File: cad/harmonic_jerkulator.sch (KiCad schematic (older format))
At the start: 41 parts, among them J101 JACK_IN, J102 JACK_OUT, J103 CONN_PSU, J105 PNP, J106 NPN, J107 SW_BYPASS, J108 DIODE1, J109 SW_DIODE, J110 DIODE2, J111 CONN_CONN_BOARD, J112 SW_DIODE, J113 CONN_CIRCUIT_BOARD, K101 TQ2SA-5V, Q101 BC850, Q102 BC856, Q103 DTC123Y, Q104 DTC123Y, U101 4013

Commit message: Corrected schematic : serial resistors on relay coil. Started layout.
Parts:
- added R112, R113: 150, Resistors_SMD:R_0805, symbol R
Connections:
- net labels removed: +BATT
- wire segments 137 -> 138
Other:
- moved on the sheet: D103, J107, K101, Q103, R106, R107, U101A

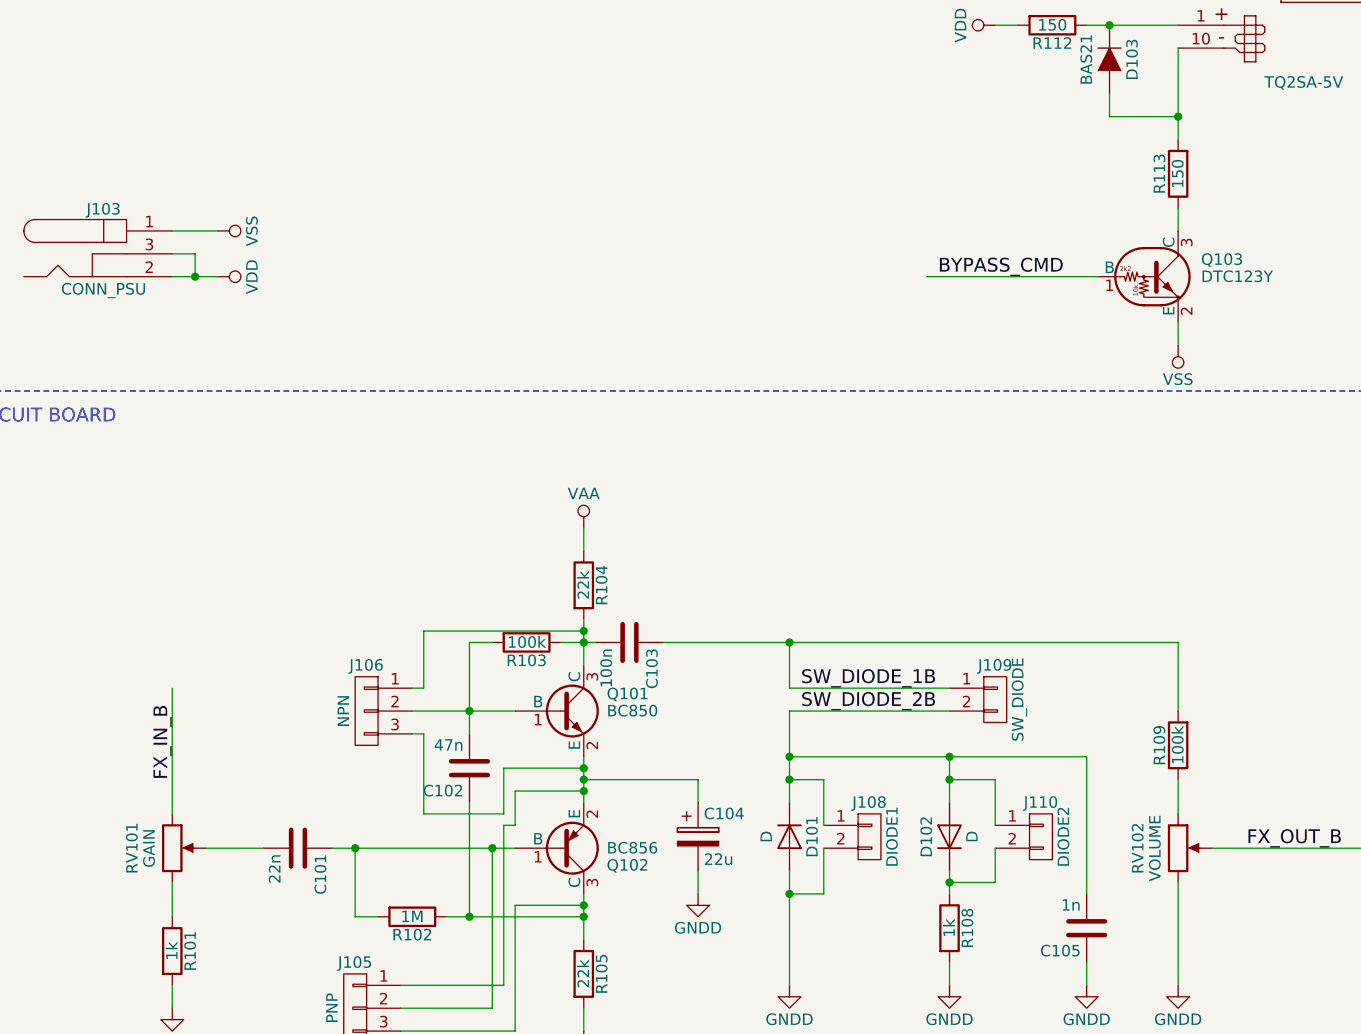
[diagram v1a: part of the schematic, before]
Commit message: Corrected pots polarity.
Connected GND and VSS.
Done single-side layout on Connectors board.
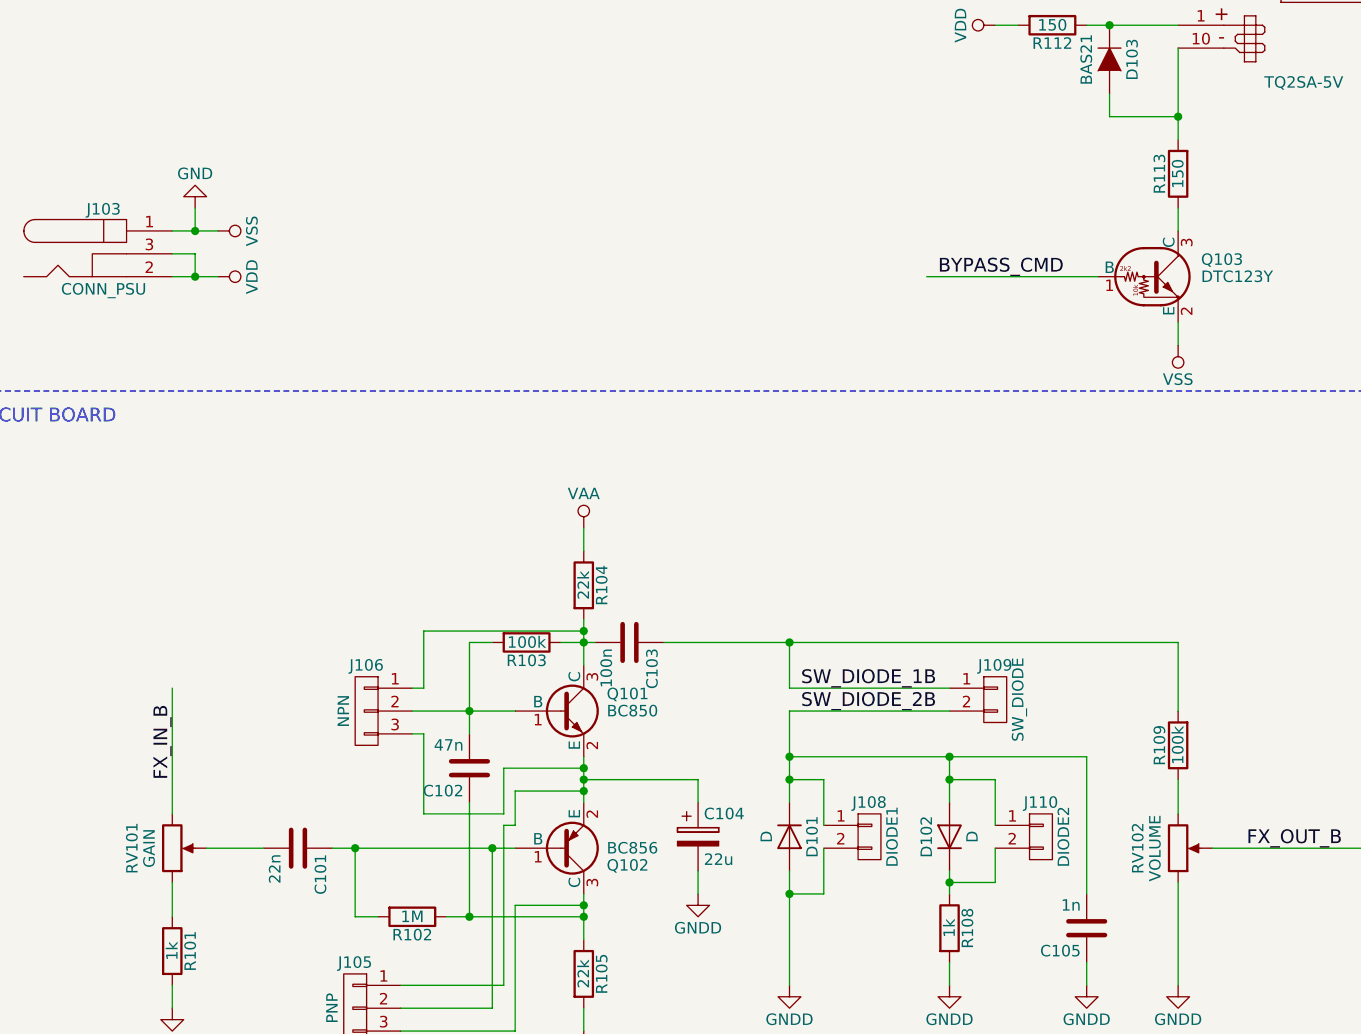
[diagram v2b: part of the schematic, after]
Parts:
- J103: footprint Connect:JACK_ALIM -> Connect:BARREL_JACK
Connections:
- wire segments 138 -> 139
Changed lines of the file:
@@
 LIBS:contrib
 LIBS:valves
+LIBS:flax_lib
 LIBS:harmonic_jerkulator-cache
 EELAYER 25 0
@@
 F 0 "J103" H 1200 3995 50  0000 C CNN
 F 1 "CONN_PSU" H 1200 3645 50  0000 C CNN
-F 2 "Connect:JACK_ALIM" H 1200 3800 50  0001 C CNN
+F 2 "Connect:BARREL_JACK" H 1200 3800 50  0001 C CNN
 F 3 "" H 1200 3800 50  0001 C CNN
 	1    1200 3800
@@
 F 3 "" H 1500 6400 50  0001 C CNN
 	1    1500 6400
-	1    0    0    -1
+	1    0    0    1
 $EndComp
 $Comp
@@
 F 3 "" H 5900 6400 50  0001 C CNN
 	1    5900 6400
-	1    0    0    -1
+	1    0    0    1
 $EndComp
 $Comp
@@
 	10500 5900 10400 5900
 Connection ~ 10400 5900
+$Comp
+L GND #PWR030
+U 1 1 59A57141
+P 1600 3600
+F 0 "#PWR030" H 1600 3350 50  0001 C CNN
+F 1 "GND" H 1600 3450 50  0000 C CNN
+F 2 "" H 1600 3600 50  0001 C CNN
+F 3 "" H 1600 3600 50  0001 C CNN
+	1    1600 3600
+	-1   0    0    1
+$EndComp
+Wire Wire Line
+	1600 3600 1600 3700
+Connection ~ 1600 3700
 $EndSCHEMATC

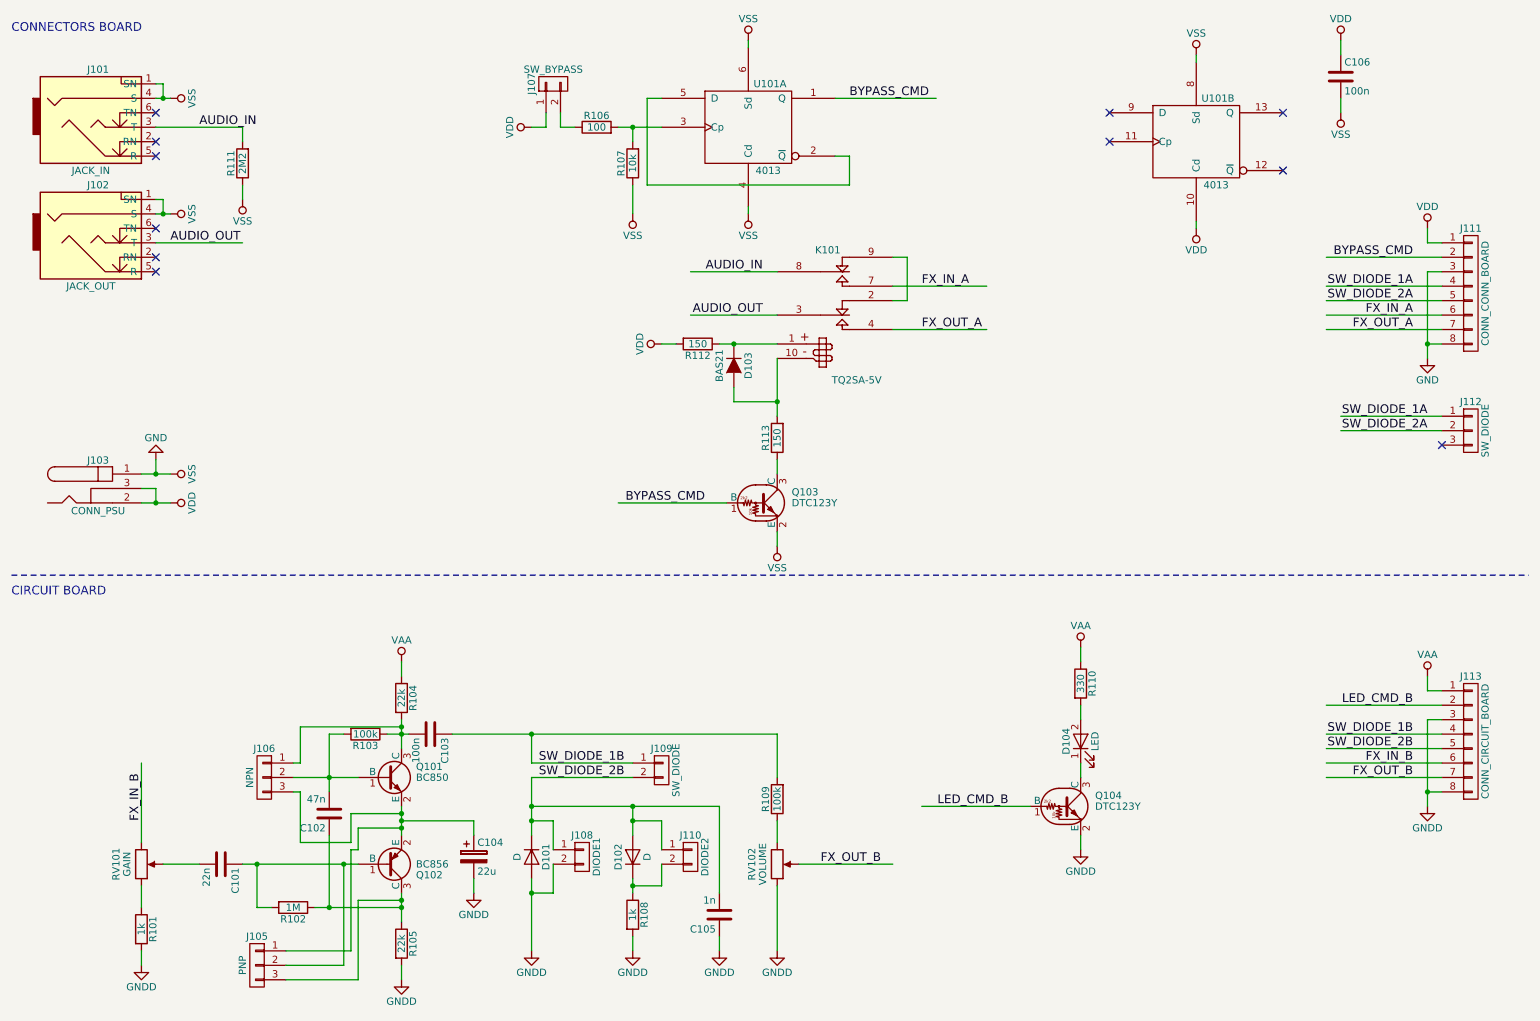
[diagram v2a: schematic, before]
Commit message: Corrections on schematic. Not finished.
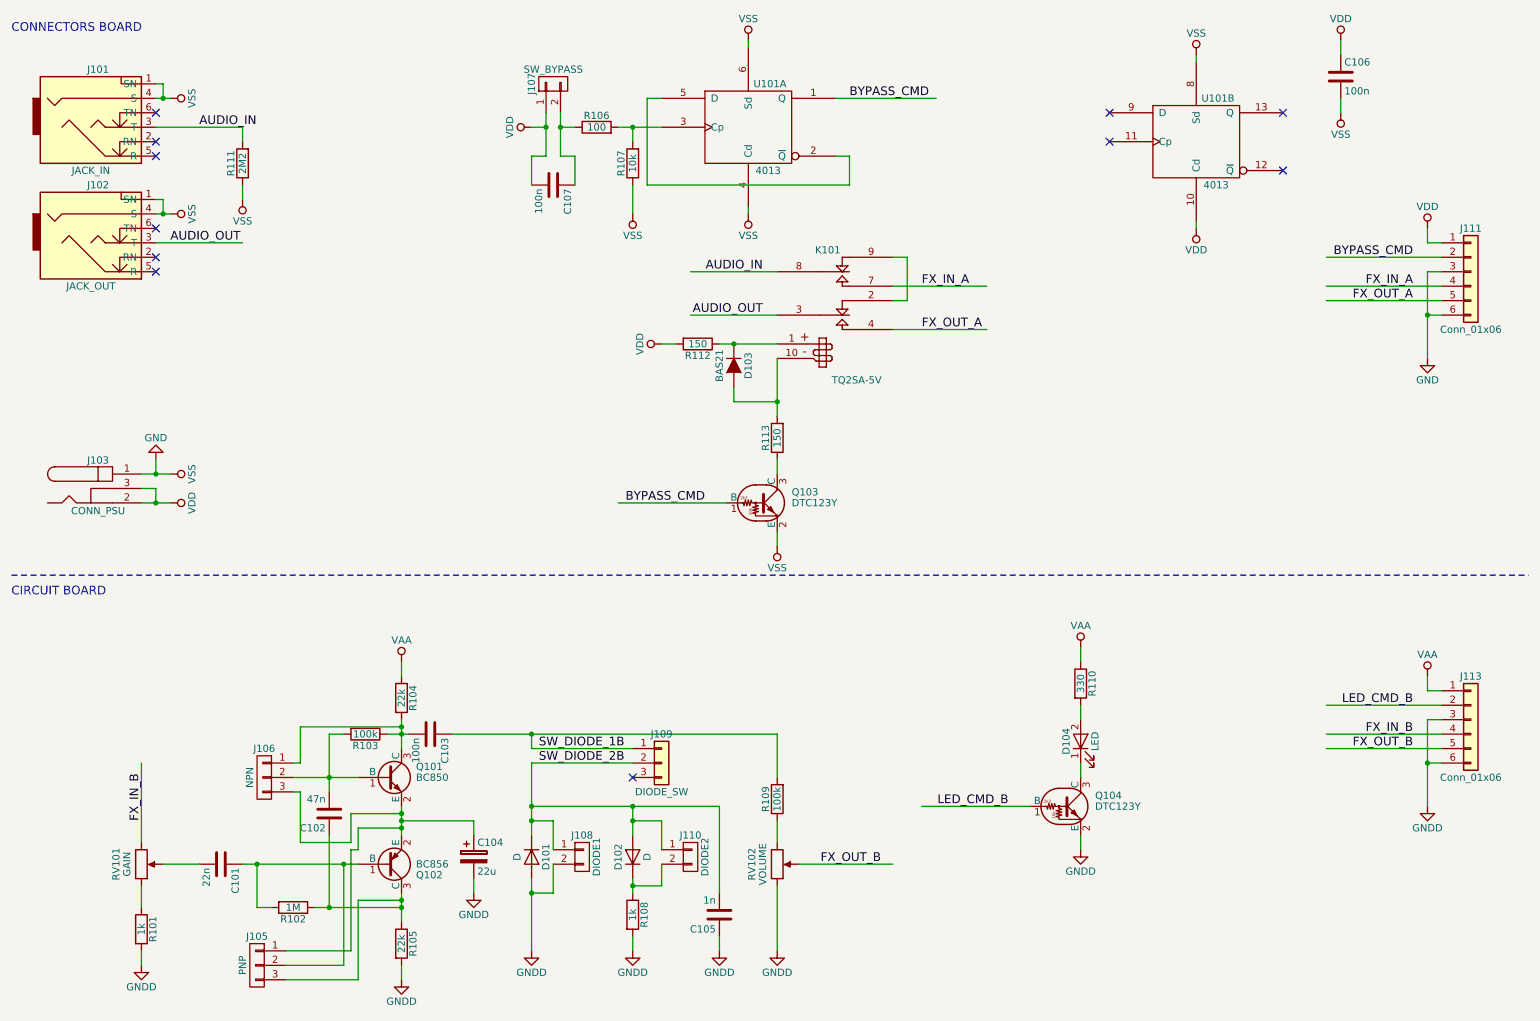
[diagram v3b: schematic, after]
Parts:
- removed J109: SW_DIODE, Pin_Headers:Pin_Header_Straight_1x02_Pitch2.54mm, symbol CONN_01X02
- removed J111: CONN_CONN_BOARD, Pin_Headers:Pin_Header_Straight_1x08_Pitch2.54mm, symbol CONN_01X08
- removed J112: SW_DIODE, Pin_Headers:Pin_Header_Straight_1x03_Pitch2.54mm, symbol CONN_01X03
- removed J113: CONN_CIRCUIT_BOARD, Pin_Headers:Pin_Header_Straight_1x08_Pitch2.54mm, symbol CONN_01X08
- added C107: 100n, Capacitors_SMD:C_0603, symbol C
- added J109: DIODE_SW, Pin_Headers:Pin_Header_Straight_1x03_Pitch2.54mm, symbol Conn_01x03
- added J111, J113: Conn_01x06, Pin_Headers:Pin_Header_Straight_1x06_Pitch2.54mm, symbol Conn_01x06
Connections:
- net labels removed: SW_DIODE_1A, SW_DIODE_2A
- wire segments 139 -> 137
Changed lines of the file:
@@
-$EndComp
-$Comp
-L CONN_01X08 J111
-U 1 1 599CA674
-P 10700 2450
-F 0 "J111" H 10700 2900 50  0000 C CNN
-F 1 "CONN_CONN_BOARD" V 10800 2450 50  0000 C CNN
-F 2 "Pin_Headers:Pin_Header_Straight_1x08_Pitch2.54mm" H 10700 2450 50  0001 C CNN
-F 3 "" H 10700 2450 50  0001 C CNN
-	1    10700 2450
-	1    0    0    -1
-$EndComp
-$Comp
-L CONN_01X08 J113
-U 1 1 599CA9F3
-P 10700 5550
-F 0 "J113" H 10700 6000 50  0000 C CNN
-F 1 "CONN_CIRCUIT_BOARD" V 10800 5550 50  0000 C CNN
-F 2 "Pin_Headers:Pin_Header_Straight_1x08_Pitch2.54mm" H 10700 5550 50  0001 C CNN
-F 3 "" H 10700 5550 50  0001 C CNN
-	1    10700 5550
-	1    0    0    -1
 $EndComp
 $Comp
@@
 Text Label 6200 6400 0    60   ~ 0
 FX_OUT_B
-Text Label 10300 5700 2    60   ~ 0
+Text Label 10300 5500 2    60   ~ 0
 FX_IN_B
-Text Label 10300 5800 2    60   ~ 0
+Text Label 10300 5600 2    60   ~ 0
 FX_OUT_B
 Text Label 10300 5300 2    60   ~ 0
@@
 	1    0    0    -1
 $EndComp
-Text Label 10300 2600 2    60   ~ 0
+Text Label 10300 2400 2    60   ~ 0
 FX_IN_A
-Text Label 10300 2700 2    60   ~ 0
+Text Label 10300 2500 2    60   ~ 0
 FX_OUT_A
 $Comp
@@
 NoConn ~ 8200 1400
 NoConn ~ 8200 1200
-$Comp
-L CONN_01X02 J109
-U 1 1 599D80DD
-P 5100 5750
-F 0 "J109" H 5100 5900 50  0000 C CNN
-F 1 "SW_DIODE" V 5200 5750 50  0000 C CNN
-F 2 "Pin_Headers:Pin_Header_Straight_1x02_Pitch2.54mm" H 5100 5750 50  0001 C CNN
-F 3 "" H 5100 5750 50  0001 C CNN
-	1    5100 5750
-	1    0    0    -1
-$EndComp
+Text Label 4250 5600 0    60   ~ 0
+SW_DIODE_1B
 Text Label 4250 5700 0    60   ~ 0
-SW_DIODE_1B
-Text Label 4250 5800 0    60   ~ 0
 SW_DIODE_2B
-Text Label 10300 5500 2    60   ~ 0
-SW_DIODE_1B
-Text Label 10300 5600 2    60   ~ 0
-SW_DIODE_2B
-Text Label 10300 2400 2    60   ~ 0
-SW_DIODE_1A
-Text Label 10300 2500 2    60   ~ 0
-SW_DIODE_2A
 $Comp
 L VSS #PWR021
@@
 Text Label 5800 2600 2    60   ~ 0
 AUDIO_OUT
-$Comp
-L CONN_01X03 J112
-U 1 1 599E0F67
-P 10700 3400
-F 0 "J112" H 10700 3600 50  0000 C CNN
-F 1 "SW_DIODE" V 10800 3400 50  0000 C CNN
-F 2 "Pin_Headers:Pin_Header_Straight_1x03_Pitch2.54mm" H 10700 3400 50  0001 C CNN
-F 3 "" H 10700 3400 50  0001 C CNN
-	1    10700 3400
-	1    0    0    -1
-$EndComp
-Text Label 10400 3300 2    60   ~ 0
-SW_DIODE_1A
-Text Label 10400 3400 2    60   ~ 0
-SW_DIODE_2A
-NoConn ~ 10500 3500
 Text Label 1900 1300 0    60   ~ 0
 AUDIO_IN
@@
 Connection ~ 4200 6600
 Wire Wire Line
-	4200 6200 4200 5800
-Wire Wire Line
-	4200 5800 4900 5800
+	4200 5700 4200 6200
+Wire Wire Line
+	4200 5700 4900 5700
 Wire Wire Line
 	4350 6300 4350 6100
@@
 	5900 5500 3650 5500
 Wire Wire Line
-	4200 5700 4900 5700
-Wire Wire Line
-	4200 5700 4200 5500
+	4200 5600 4900 5600
 Connection ~ 4200 5500
 Wire Wire Line
@@
 	9700 5500 10500 5500
 Wire Wire Line
-	9700 5700 10500 5700
-Wire Wire Line
 	8000 4900 8000 5000
 Wire Wire Line
@@
 	9700 2400 10500 2400
 Wire Wire Line
-	9700 2600 10500 2600
-Wire Wire Line
 	9800 1100 9800 1200
 Wire Wire Line
@@
 	10500 5600 9700 5600
 Wire Wire Line
-	10500 5800 9700 5800
-Wire Wire Line
 	10500 2500 9700 2500
-Wire Wire Line
-	9700 2700 10500 2700
 Wire Wire Line
 	5700 1850 5700 1900
@@
 	4900 1700 4900 1900
 Wire Wire Line
-	4400 1200 4400 1300
+	4400 1200 4400 1500
 Wire Wire Line
 	4400 1300 4500 1300
@@
 	4200 1300 4300 1300
 Wire Wire Line
-	4300 1300 4300 1200
+	4300 1200 4300 1500
 Wire Wire Line
 	5500 2800 5900 2800
@@
 Wire Wire Line
 	5900 2600 5300 2600
-Wire Wire Line
-	10500 3400 9800 3400
-Wire Wire Line
-	10500 3300 9800 3300
 Wire Wire Line
 	1600 1300 2200 1300
@@
 	10400 2300 10400 2900
 Wire Wire Line
-	10500 2800 10400 2800
-Connection ~ 10400 2800
-Wire Wire Line
 	10500 5300 9700 5300
 Wire Wire Line
@@
 Wire Wire Line
 	10400 5400 10400 6000
-Wire Wire Line
-	10500 5900 10400 5900
-Connection ~ 10400 5900
 $Comp
 L GND #PWR030
@@
 	1600 3600 1600 3700
 Connection ~ 1600 3700
+$Comp
+L Conn_01x06 J111
+U 1 1 5A410A19
+P 10700 2300
+F 0 "J111" H 10700 2600 50  0000 C CNN
+F 1 "Conn_01x06" H 10700 1900 50  0000 C CNN
+F 2 "Pin_Headers:Pin_Header_Straight_1x06_Pitch2.54mm" H 10700 2300 50  0001 C CNN
+F 3 "" H 10700 2300 50  0001 C CNN
+	1    10700 2300
+	1    0    0    -1
+$EndComp
+Wire Wire Line
+	10500 2600 10400 2600
+Connection ~ 10400 2600
+$Comp
+L C C107
+U 1 1 5A411408
+P 4350 1700
+F 0 "C107" H 4375 1800 50  0000 L CNN
+F 1 "100n" H 4375 1600 50  0000 L CNN
+F 2 "Capacitors_SMD:C_0603" H 4388 1550 50  0001 C CNN
+F 3 "" H 4350 1700 50  0001 C CNN
+	1    4350 1700
+	0    1    1    0
+$EndComp
+Wire Wire Line
+	4500 1700 4500 1500
+Wire Wire Line
+	4500 1500 4400 1500
+Connection ~ 4400 1300
+Wire Wire Line
+	4300 1500 4200 1500
+Wire Wire Line
+	4200 1500 4200 1700
+Connection ~ 4300 1300
+$Comp
+L Conn_01x06 J113
+U 1 1 5A4124BB
+P 10700 5400
+F 0 "J113" H 10700 5700 50  0000 C CNN
+F 1 "Conn_01x06" H 10700 5000 50  0000 C CNN
+F 2 "Pin_Headers:Pin_Header_Straight_1x06_Pitch2.54mm" H 10700 5400 50  0001 C CNN
+F 3 "" H 10700 5400 50  0001 C CNN
+	1    10700 5400
+	1    0    0    -1
+$EndComp
+Wire Wire Line
+	10500 5700 10400 5700
+Connection ~ 10400 5700
+Wire Wire Line
+	4200 5600 4200 5500
+$Comp
+L Conn_01x03 J109
+U 1 1 5A413622
+P 5100 5700
+F 0 "J109" H 5100 5900 50  0000 C CNN
+F 1 "DIODE_SW" H 5100 5500 50  0000 C CNN
+F 2 "Pin_Headers:Pin_Header_Straight_1x03_Pitch2.54mm" H 5100 5700 50  0001 C CNN
+F 3 "" H 5100 5700 50  0001 C CNN
+	1    5100 5700
+	1    0    0    -1
+$EndComp
+NoConn ~ 4900 5800
 $EndSCHEMATC
